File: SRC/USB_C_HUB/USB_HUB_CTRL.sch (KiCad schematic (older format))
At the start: 27 parts

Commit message: commit with all DFPs properly connected
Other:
- moved on the sheet: C?, U?

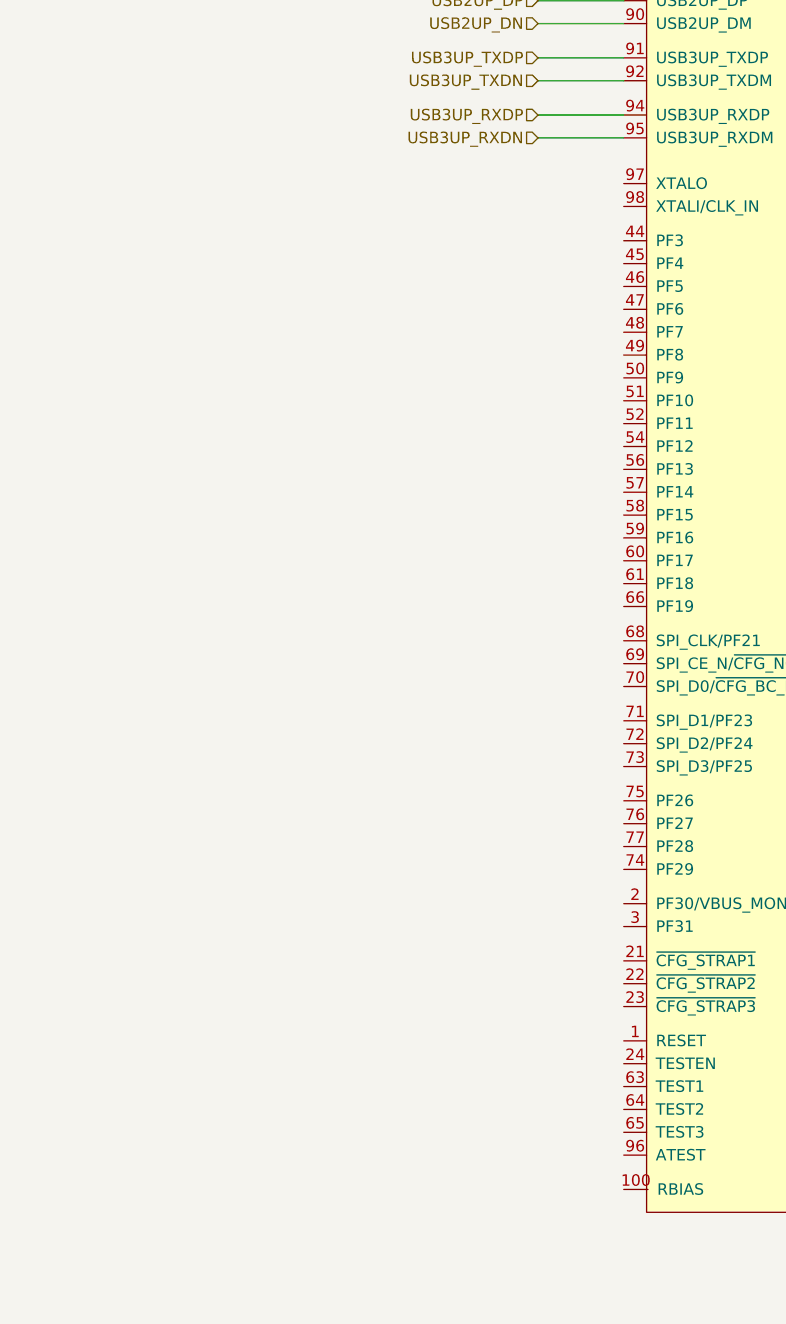
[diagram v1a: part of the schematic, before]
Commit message: all but HDMI + 2 DFP ports
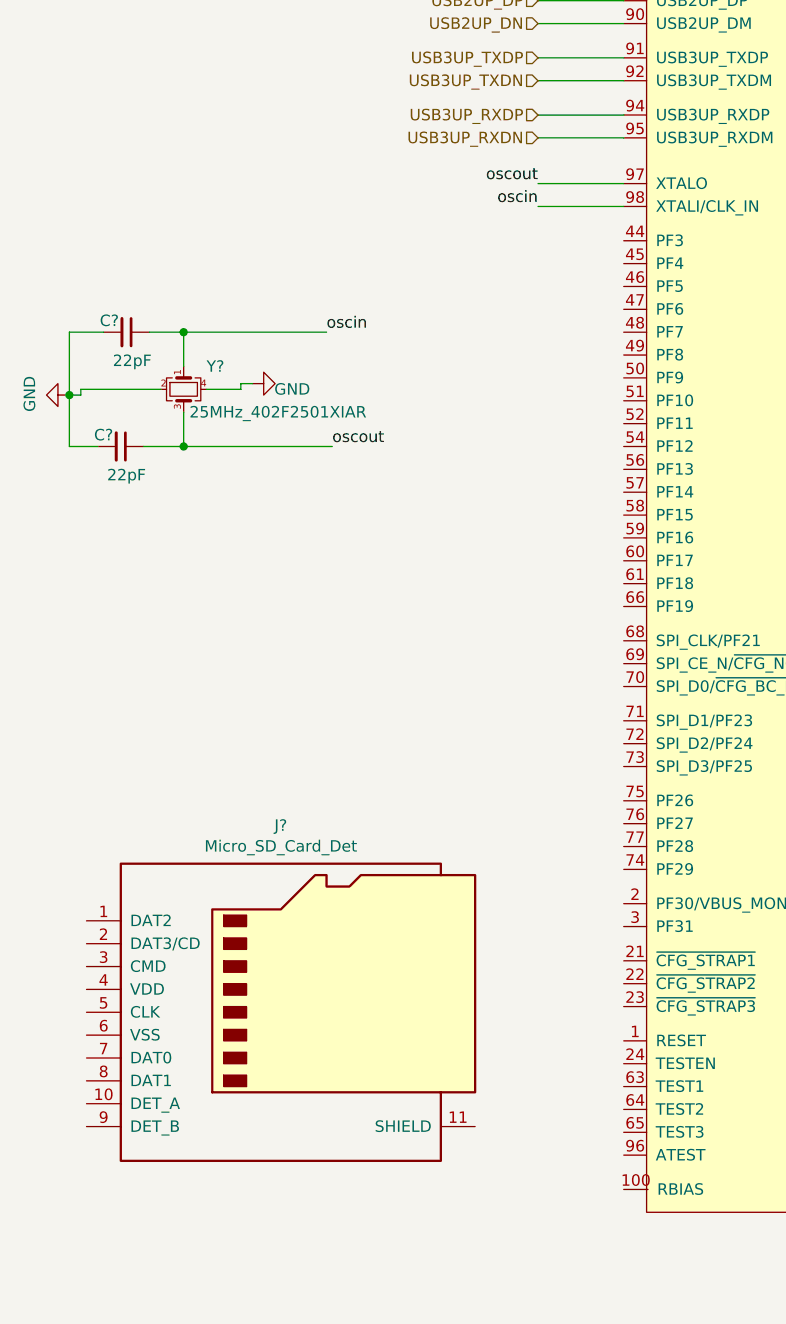
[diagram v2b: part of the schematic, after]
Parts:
- added C? (x2): 22pF, symbol Device:C_Small
- added J?: Micro_SD_Card_Det, symbol Connector:Micro_SD_Card_Det
- added Y?: 25MHz_402F2501XIAR, symbol Device:Crystal_GND24_Small
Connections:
- net GND: now also C?.2, C?.2, Y?.2, Y?.4
- net oscout: now reaches U?.97 (XTALO)
- net oscout: now also C?.1, Y?.3
- net oscin: now reaches U?.98 (XTALI/CLK_IN)
- net oscin: now also C?.1, Y?.1
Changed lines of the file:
@@
 $Descr A4 11693 8268
 encoding utf-8
-Sheet 5 7
+Sheet 5 9
 Title ""
 Date ""
@@
 NoConn ~ 6575 6100
 NoConn ~ 6575 6200
+$Comp
+L Connector:Micro_SD_Card_Det J?
+U 1 1 65C685B8
+P 2125 5975
+F 0 "J?" H 2075 6792 50  0000 C CNN
+F 1 "Micro_SD_Card_Det" H 2075 6701 50  0000 C CNN
+F 2 "" H 4175 6675 50  0001 C CNN
+F 3 "https://www.hirose.com/product/en/download_file/key_name/DM3/category/Catalog/doc_file_id/49662/?file_category_id=4&item_id=195&is_series=1" H 2125 6075 50  0001 C CNN
+	1    2125 5975
+	1    0    0    -1
+$EndComp
+Wire Wire Line
+	1300 3000 1150 3000
+Connection ~ 1650 3000
+Wire Wire Line
+	1650 3000 2275 3000
+Wire Wire Line
+	1500 3000 1650 3000
+Connection ~ 1650 3500
+Wire Wire Line
+	1650 3500 2300 3500
+Wire Wire Line
+	1150 3275 1150 3500
+Connection ~ 1150 3275
+$Comp
+L OLIMEX_Power:GND #PWR?
+U 1 1 65D01721
+P 1150 3275
+AR Path="/619540C6/65D01721" Ref="#PWR?"  Part="1"
+AR Path="/65D01721" Ref="#PWR?"  Part="1"
+AR Path="/631C6BCF/65D01721" Ref="#PWR?"  Part="1"
+F 0 "#PWR?" H 1150 3025 50  0001 C CNN
+F 1 "GND" H 1155 3102 50  0000 C CNN
+F 2 "" H 1150 3275 60  0000 C CNN
+F 3 "" H 1150 3275 60  0000 C CNN
+	1    1150 3275
+	0    1    -1   0
+$EndComp
+Wire Wire Line
+	1150 3500 1275 3500
+Wire Wire Line
+	1150 3000 1150 3275
+Wire Wire Line
+	1650 3000 1650 3150
+Wire Wire Line
+	1650 3500 1650 3350
+Wire Wire Line
+	1475 3500 1650 3500
+$Comp
+L Device:C_Small C?
+U 1 1 65D0172C
+P 1400 3000
+AR Path="/65D0172C" Ref="C?"  Part="1"
+AR Path="/631C6BCF/65D0172C" Ref="C?"  Part="1"
+F 0 "C?" V 1350 2925 50  0000 C CNN
+F 1 "22pF" V 1525 3025 50  0000 C CNN
+F 2 "" H 1400 3000 50  0001 C CNN
+F 3 "~" H 1400 3000 50  0001 C CNN
+	1    1400 3000
+	0    1    1    0
+$EndComp
+$Comp
+L Device:Crystal_GND24_Small Y?
+U 1 1 65D01733
+P 1650 3250
+AR Path="/65D01733" Ref="Y?"  Part="1"
+AR Path="/631C6BCF/65D01733" Ref="Y?"  Part="1"
+F 0 "Y?" V 1550 3350 50  0000 L CNN
+F 1 "25MHz_402F2501XIAR" V 1750 3275 50  0000 L CNN
+F 2 "" H 1650 3250 50  0001 C CNN
+F 3 "~" H 1650 3250 50  0001 C CNN
+F 4 "402F2501XIAR" H 1650 3250 50  0001 C CNN "Mfr No."
+	1    1650 3250
+	0    1    1    0
+$EndComp
+$Comp
+L Device:C_Small C?
+U 1 1 65D01739
+P 1375 3500
+AR Path="/65D01739" Ref="C?"  Part="1"
+AR Path="/631C6BCF/65D01739" Ref="C?"  Part="1"
+F 0 "C?" V 1325 3425 50  0000 C CNN
+F 1 "22pF" V 1500 3525 50  0000 C CNN
+F 2 "" H 1375 3500 50  0001 C CNN
+F 3 "~" H 1375 3500 50  0001 C CNN
+	1    1375 3500
+	0    1    1    0
+$EndComp
+Wire Wire Line
+	1550 3250 1200 3250
+Wire Wire Line
+	1200 3250 1200 3275
+Wire Wire Line
+	1150 3275 1200 3275
+$Comp
+L OLIMEX_Power:GND #PWR?
+U 1 1 65D01742
+P 1950 3225
+AR Path="/619540C6/65D01742" Ref="#PWR?"  Part="1"
+AR Path="/65D01742" Ref="#PWR?"  Part="1"
+AR Path="/631C6BCF/65D01742" Ref="#PWR?"  Part="1"
+F 0 "#PWR?" H 1950 2975 50  0001 C CNN
+F 1 "GND" V 1975 3050 50  0000 C CNN
+F 2 "" H 1950 3225 60  0000 C CNN
+F 3 "" H 1950 3225 60  0000 C CNN
+	1    1950 3225
+	0    -1   1    0
+$EndComp
+Wire Wire Line
+	1750 3250 1900 3250
+Wire Wire Line
+	1900 3250 1900 3225
+Wire Wire Line
+	1900 3225 1950 3225
+Text Label 2275 3000 0    50   ~ 0
+oscin
+Text Label 3200 2450 2    50   ~ 0
+oscin
+Text Label 2300 3500 0    50   ~ 0
+oscout
+Text Label 3200 2350 2    50   ~ 0
+oscout
+Wire Wire Line
+	3575 2350 3200 2350
+Wire Wire Line
+	3575 2450 3200 2450
 $EndSCHEMATC

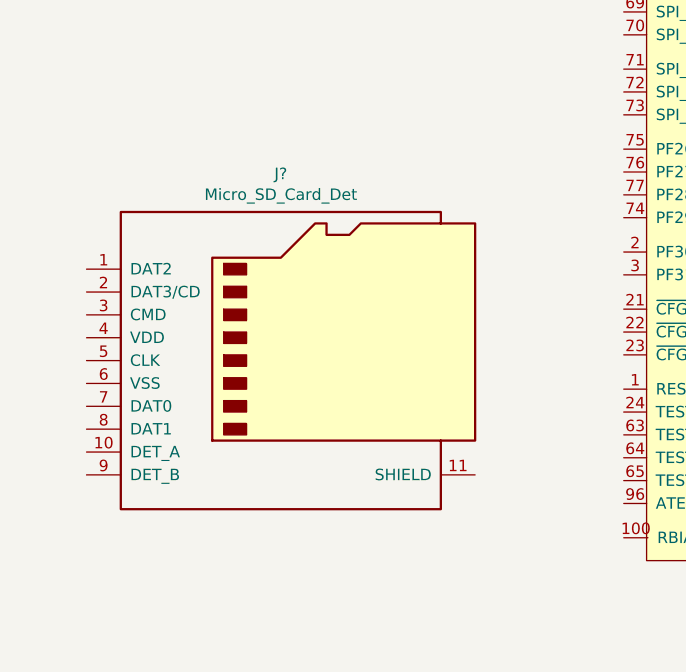
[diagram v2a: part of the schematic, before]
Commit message: all but HDMI + 2 DFP ports
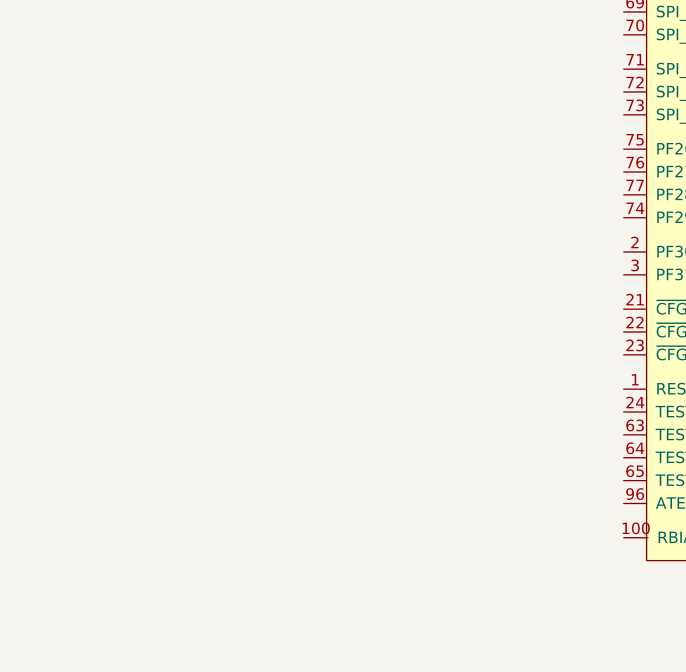
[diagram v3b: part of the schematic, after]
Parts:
- removed J?: Micro_SD_Card_Det, symbol Connector:Micro_SD_Card_Det
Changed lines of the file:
@@
 NoConn ~ 6575 6100
 NoConn ~ 6575 6200
-$Comp
-L Connector:Micro_SD_Card_Det J?
-U 1 1 65C685B8
-P 2125 5975
-F 0 "J?" H 2075 6792 50  0000 C CNN
-F 1 "Micro_SD_Card_Det" H 2075 6701 50  0000 C CNN
-F 2 "" H 4175 6675 50  0001 C CNN
-F 3 "https://www.hirose.com/product/en/download_file/key_name/DM3/category/Catalog/doc_file_id/49662/?file_category_id=4&item_id=195&is_series=1" H 2125 6075 50  0001 C CNN
-	1    2125 5975
-	1    0    0    -1
-$EndComp
 Wire Wire Line
 	1300 3000 1150 3000
@@
 AR Path="/65D01721" Ref="#PWR?"  Part="1"
 AR Path="/631C6BCF/65D01721" Ref="#PWR?"  Part="1"
+AR Path="/6214F1F1/65D01721" Ref="#PWR?"  Part="1"
 F 0 "#PWR?" H 1150 3025 50  0001 C CNN
 F 1 "GND" H 1155 3102 50  0000 C CNN
@@
 AR Path="/65D0172C" Ref="C?"  Part="1"
 AR Path="/631C6BCF/65D0172C" Ref="C?"  Part="1"
+AR Path="/6214F1F1/65D0172C" Ref="C?"  Part="1"
 F 0 "C?" V 1350 2925 50  0000 C CNN
 F 1 "22pF" V 1525 3025 50  0000 C CNN
@@
 AR Path="/65D01733" Ref="Y?"  Part="1"
 AR Path="/631C6BCF/65D01733" Ref="Y?"  Part="1"
+AR Path="/6214F1F1/65D01733" Ref="Y?"  Part="1"
 F 0 "Y?" V 1550 3350 50  0000 L CNN
 F 1 "25MHz_402F2501XIAR" V 1750 3275 50  0000 L CNN
@@
 AR Path="/65D01739" Ref="C?"  Part="1"
 AR Path="/631C6BCF/65D01739" Ref="C?"  Part="1"
+AR Path="/6214F1F1/65D01739" Ref="C?"  Part="1"
 F 0 "C?" V 1325 3425 50  0000 C CNN
 F 1 "22pF" V 1500 3525 50  0000 C CNN
@@
 AR Path="/65D01742" Ref="#PWR?"  Part="1"
 AR Path="/631C6BCF/65D01742" Ref="#PWR?"  Part="1"
+AR Path="/6214F1F1/65D01742" Ref="#PWR?"  Part="1"
 F 0 "#PWR?" H 1950 2975 50  0001 C CNN
 F 1 "GND" V 1975 3050 50  0000 C CNN

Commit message: ALL DONE BUT THE HDMI SECTION. NEED FOOTPRINT ASSIGNMENT
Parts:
- added C39: 1uF, symbol Device:C_Small
- added R30: 1K, symbol Device:R_US
- added R31, R32, R33, R34, R37, R46, R52: 10K, symbol Device:R_US
- added R35, R36, R38, R39: 200K, symbol Device:R_US
- added R40, R41, R42, R43, R44, R45, R47, R48, R49, R50, R51: 47K, symbol Device:R_US
- added R53: 12K, symbol Device:R_US
- gave numbers to parts that had none: 30
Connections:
- net +3V3: now also C39.1, R31.2, R32.2, R33.2, R34.2, R52.2
- net GND: now also U9.24 (TESTEN), C39.2, R30.2, R35.2, R36.2, R37.2, R38.2, R39.2, R40.2, R41.2, R42.2, R43.2, R44.2, R45.2, R46.2, R47.2, R48.2, R49.2, R50.2, R51.2, R53.2
- net at U9.1 (RESET): now also R31.1
- net at U9.100 (RBIAS): now also R53.1
- net at U9.2 (PF30/VBUS_MON_UP): now also R52.1
- net at U9.21 (~CFG_STRAP1): now also R37.1
- net at U9.22 (~CFG_STRAP2): now also R38.1
- net at U9.23 (~CFG_STRAP3): now also R39.1
- net at U9.3 (PF31): now also R50.1
- net at U9.44 (PF3): now also R40.1
- net at U9.45 (PF4): now also R41.1
- net at U9.46 (PF5): now also R42.1
- net at U9.47 (PF6): now also R43.1
- net at U9.48 (PF7): now also R44.1
- net at U9.61 (PF18): now also R30.1
- net at U9.63 (TEST1): now also R34.1
- net at U9.64 (TEST2): now also R32.1
- net at U9.65 (TEST3): now also R33.1
- net at U9.68 (SPI_CLK/PF21): now also R51.1
- net at U9.69 (SPI_CE_N/~CFG_NON_REM/PF20): now also R45.1
- net at U9.70 (SPI_D0/~CFG_BC_EN/PF22): now also R46.1
- net at U9.71 (SPI_D1/PF23): now also R47.1
- net at U9.72 (SPI_D2/PF24): now also R48.1
- net at U9.73 (SPI_D3/PF25): now also R49.1
- net at U9.75 (PF26): now also R35.1
- net at U9.76 (PF27): now also R36.1
- no-connect marks 4 -> 17
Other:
- moved on the sheet: C32, C33, Y1

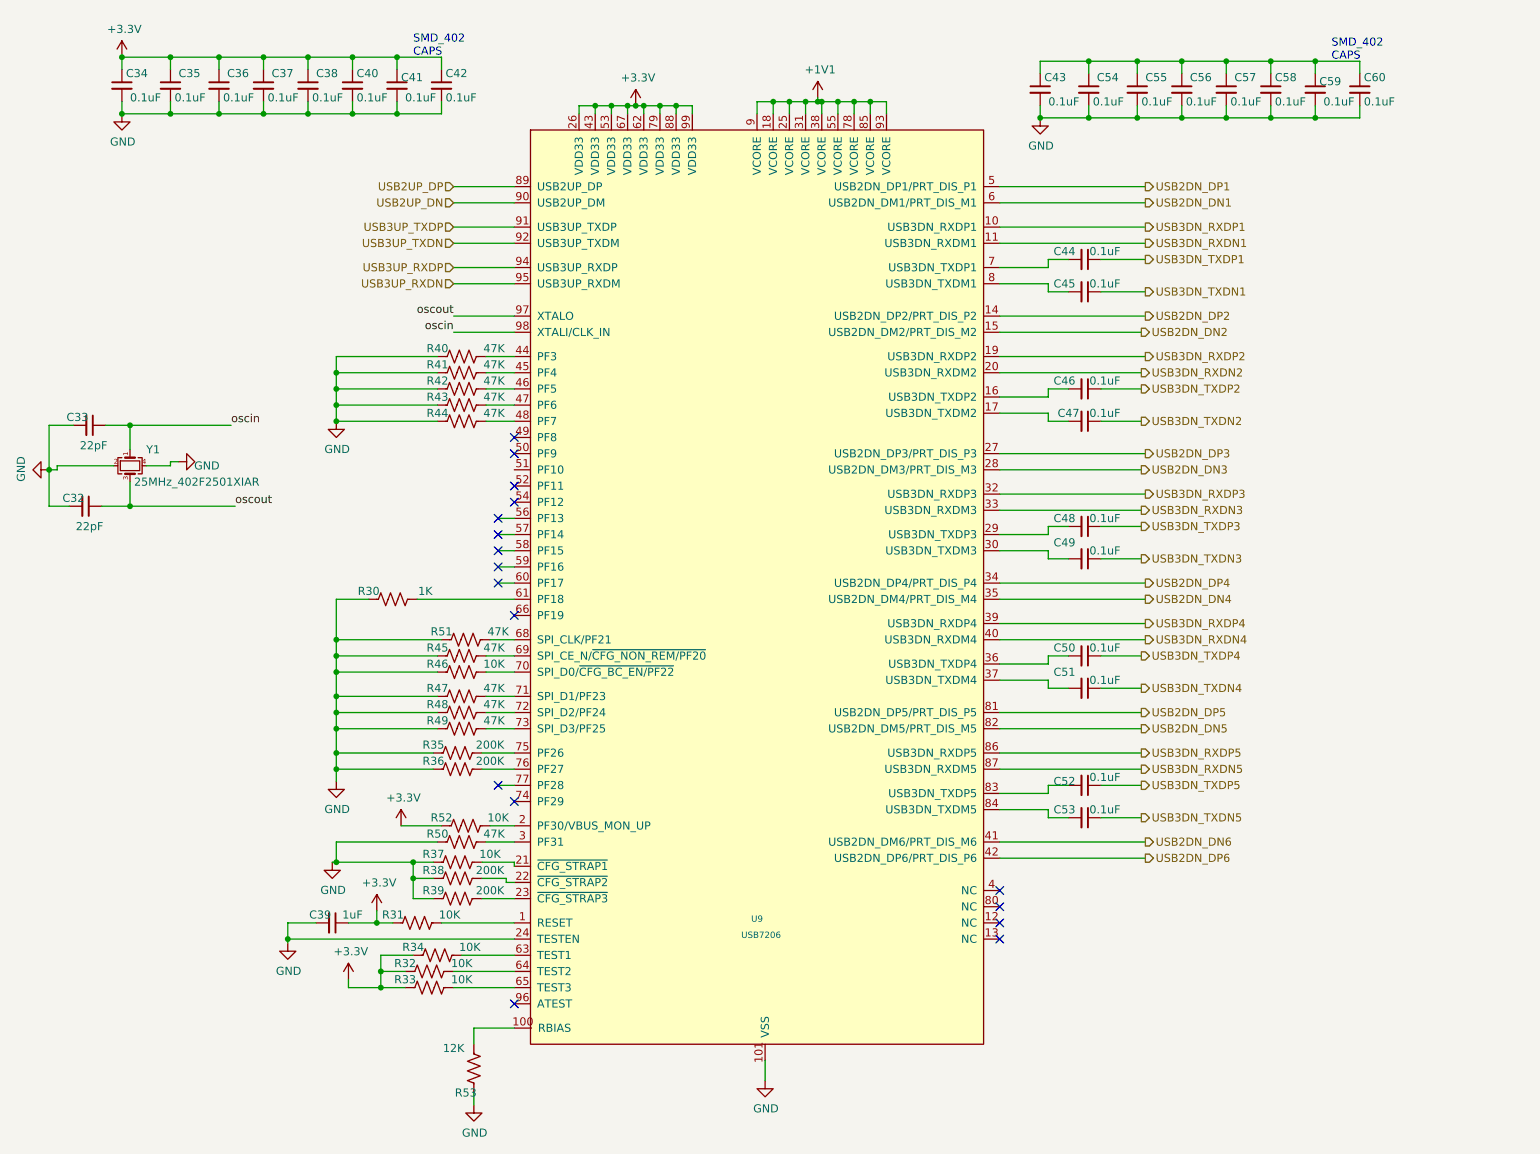
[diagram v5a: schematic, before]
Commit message: schematic capture complete. Pending Footprint assignment. accetable Errors=21
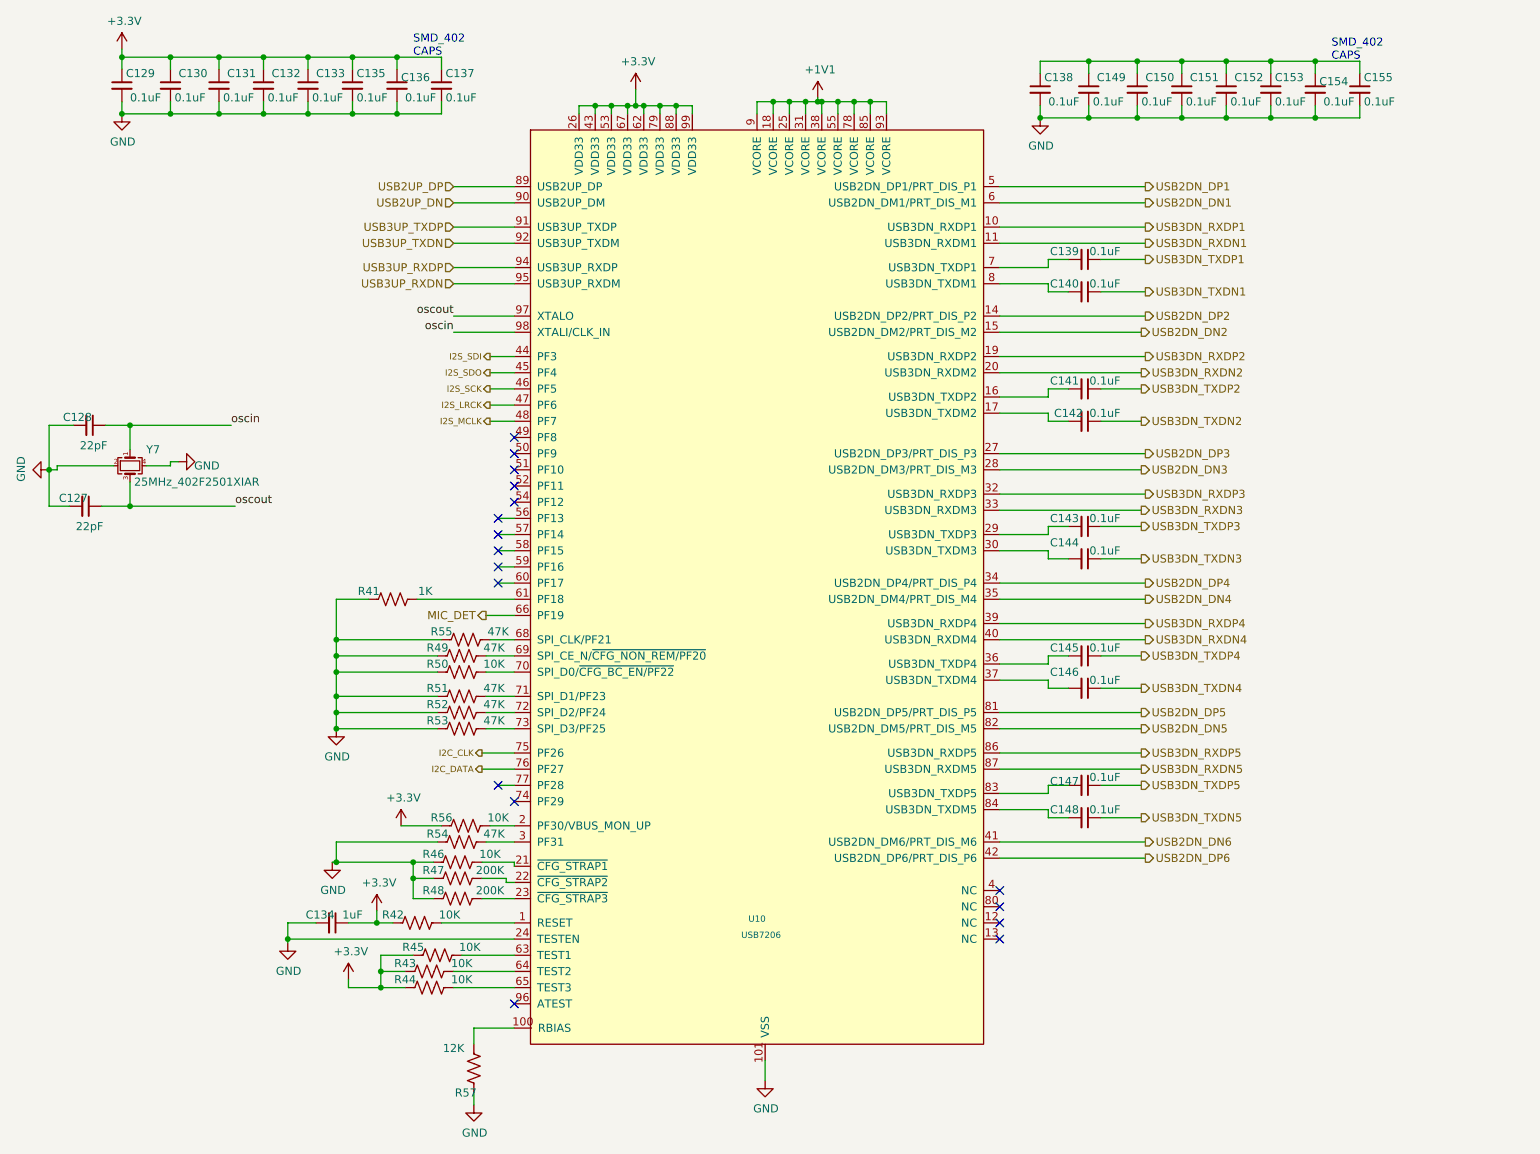
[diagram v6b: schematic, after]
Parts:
- removed R35, R36: 200K, symbol Device:R_US
- removed R40, R41, R42, R43, R44: 47K, symbol Device:R_US
- renumbered C32 to C127, C33 to C128, C34 to C129, C35 to C130, C36 to C131, C37 to C132, C38 to C133, C39 to C134, C40 to C135, C41 to C136, C42 to C137, C43 to C138, C44 to C139, C45 to C140, C46 to C141, C47 to C142, C48 to C143, C49 to C144, C50 to C145, C51 to C146, C52 to C147, C53 to C148, C54 to C149, C55 to C150, C56 to C151, C57 to C152, C58 to C153, C59 to C154, C60 to C155, R30 to R41, R31 to R42, R32 to R43, R33 to R44, R34 to R45, R37 to R46, R38 to R47, R39 to R48, R45 to R49, R46 to R50, R47 to R51, R48 to R52, R49 to R53, R50 to R54, R51 to R55, R52 to R56, R53 to R57, U9 to U10, Y1 to Y7
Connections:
- net I2S_SDI: now reaches U10.44 (PF3)
- net I2S_SDO: now reaches U10.45 (PF4)
- net I2S_SCK: now reaches U10.46 (PF5)
- net I2S_LRCK: now reaches U10.47 (PF6)
- net I2S_MCLK: now reaches U10.48 (PF7)
- net MIC_DET: now reaches U10.66 (PF19)
- net I2C_CLK: now reaches U10.75 (PF26)
- net I2C_DATA: now reaches U10.76 (PF27)
